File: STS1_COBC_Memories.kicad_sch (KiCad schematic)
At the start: 9 parts, among them J5 Conn_01x03_Male

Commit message: Set all passive components (except in the RF path) to 0603
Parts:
- C3, C4, C5, C6: footprint Capacitor_SMD:C_0805_2012Metric -> Capacitor_SMD:C_0603_1608Metric
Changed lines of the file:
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@@
     (property "Reference" "C3" (id 0) (at 118.11 40.5892 90))
     (property "Value" "100n" (id 1) (at 118.11 42.9006 90))
-    (property "Footprint" "Capacitor_SMD:C_0805_2012Metric" (id 2) (at 114.3 47.9552 0)
+    (property "Footprint" "Capacitor_SMD:C_0603_1608Metric" (id 2) (at 114.3 47.9552 0)
       (effects (font (size 1.27 1.27)) hide)
     )
@@
     (property "Reference" "C4" (id 0) (at 118.11 49.4792 90))
     (property "Value" "47u" (id 1) (at 118.11 51.7906 90))
-    (property "Footprint" "Capacitor_SMD:C_0805_2012Metric" (id 2) (at 114.3 56.8452 0)
+    (property "Footprint" "Capacitor_SMD:C_0603_1608Metric" (id 2) (at 114.3 56.8452 0)
       (effects (font (size 1.27 1.27)) hide)
     )
@@
     (property "Reference" "C5" (id 0) (at 226.06 41.8592 90))
     (property "Value" "100n" (id 1) (at 226.06 44.1706 90))
-    (property "Footprint" "Capacitor_SMD:C_0805_2012Metric" (id 2) (at 222.25 49.2252 0)
+    (property "Footprint" "Capacitor_SMD:C_0603_1608Metric" (id 2) (at 222.25 49.2252 0)
       (effects (font (size 1.27 1.27)) hide)
     )
@@
     (property "Reference" "C6" (id 0) (at 226.06 50.7492 90))
     (property "Value" "47u" (id 1) (at 226.06 53.0606 90))
-    (property "Footprint" "Capacitor_SMD:C_0805_2012Metric" (id 2) (at 222.25 58.1152 0)
+    (property "Footprint" "Capacitor_SMD:C_0603_1608Metric" (id 2) (at 222.25 58.1152 0)
       (effects (font (size 1.27 1.27)) hide)
     )

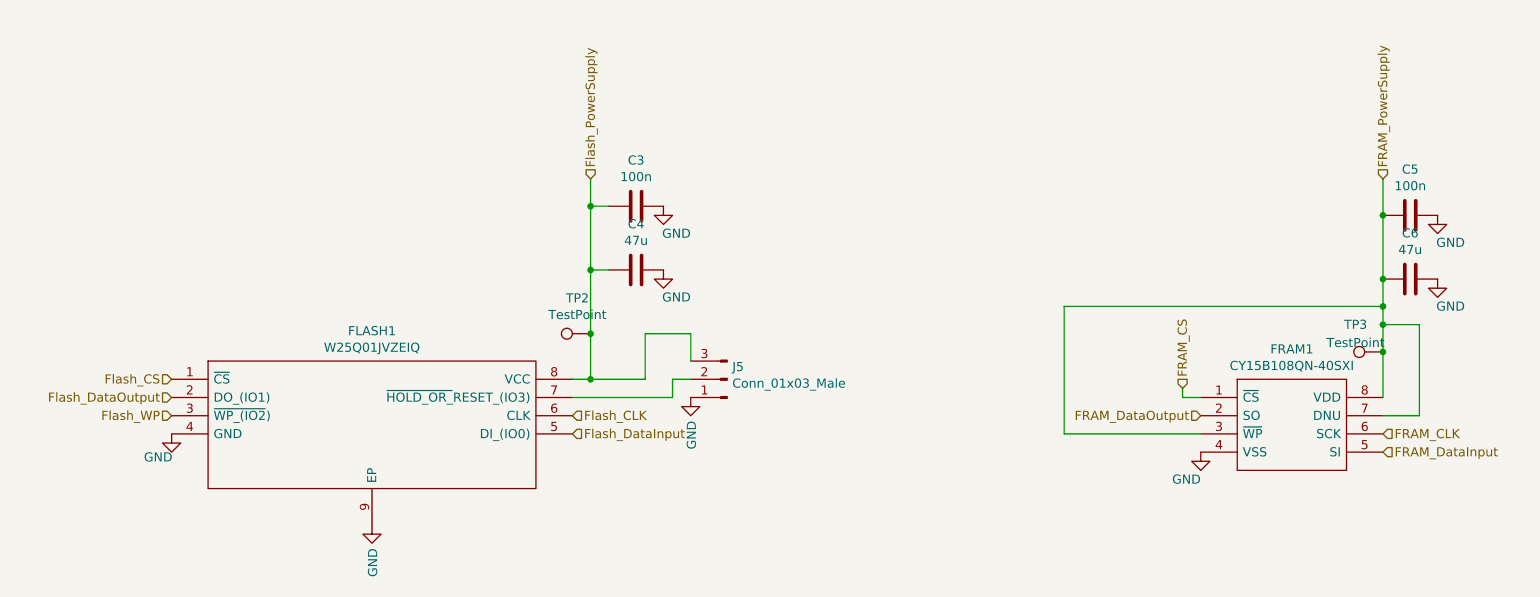
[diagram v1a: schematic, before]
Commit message: feat: clean up schematic
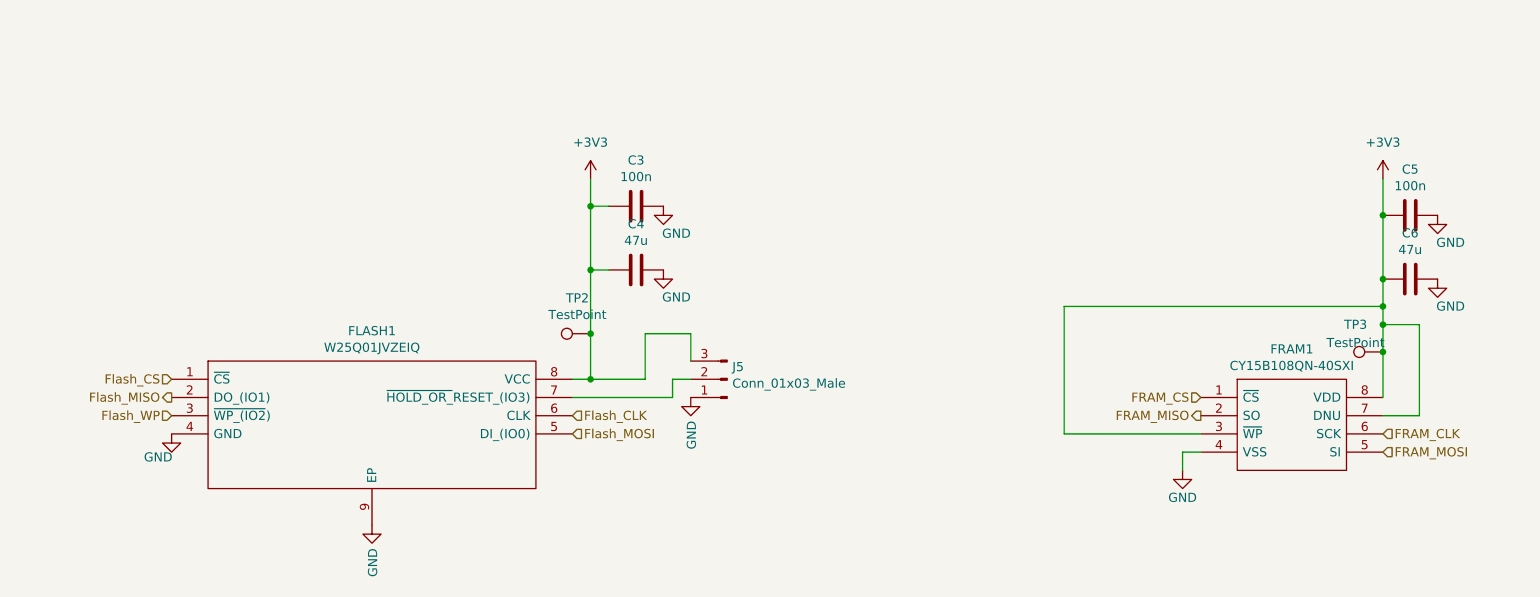
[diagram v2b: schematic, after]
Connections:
- net Flash_PowerSupply is gone; now on net +3V3: C3.2, C4.2, FLASH1.8 (VCC), J5.3 (Pin_3), TP2.1
- net FRAM_DataInput renamed FRAM_MOSI
- net FRAM_DataOutput renamed FRAM_MISO
- net FRAM_PowerSupply renamed +3V3
- net Flash_DataInput renamed Flash_MOSI
- net Flash_DataOutput renamed Flash_MISO
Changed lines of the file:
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@@
-    (stroke (width 0) (type default) (color 0 0 0 0))
-  )
-  (wire (pts (xy 196.85 73.66) (xy 194.31 73.66))
     (stroke (width 0) (type default) (color 0 0 0 0))
   )
@@
     (stroke (width 0) (type default) (color 0 0 0 0))
   )
+  (wire (pts (xy 194.31 81.28) (xy 196.85 81.28))
+    (stroke (width 0) (type default) (color 0 0 0 0))
+  )
   (wire (pts (xy 177.8 78.74) (xy 196.85 78.74))
     (stroke (width 0) (type default) (color 0 0 0 0))
@@
     (stroke (width 0) (type default) (color 0 0 0 0))
   )
-  (wire (pts (xy 194.31 72.39) (xy 194.31 73.66))
-    (stroke (width 0) (type default) (color 0 0 0 0))
-  )
   (wire (pts (xy 125.73 68.58) (xy 125.73 64.77))
     (stroke (width 0) (type default) (color 0 0 0 0))
@@
     (stroke (width 0) (type default) (color 0 0 0 0))
   )
+  (wire (pts (xy 194.31 83.82) (xy 194.31 81.28))
+    (stroke (width 0) (type default) (color 0 0 0 0))
+  )
   (wire (pts (xy 119.38 64.77) (xy 119.38 71.12))
     (stroke (width 0) (type default) (color 0 0 0 0))
@@
     (stroke (width 0) (type default) (color 0 0 0 0))
   )
-  (hierarchical_label "FRAM_CS" (shape input) (at 194.31 72.39 90)
+  (hierarchical_label "FRAM_CS" (shape input) (at 196.85 73.66 180)
+    (effects (font (size 1.27 1.27)) (justify right))
+  )
+  (hierarchical_label "FRAM_MOSI" (shape input) (at 222.25 81.28 0)
     (effects (font (size 1.27 1.27)) (justify left))
   )
-  (hierarchical_label "FRAM_PowerSupply" (shape input) (at 222.25 43.18 90)
-    (effects (font (size 1.27 1.27)) (justify left))
-  )
-  (hierarchical_label "FRAM_DataInput" (shape input) (at 222.25 81.28 0)
-    (effects (font (size 1.27 1.27)) (justify left))
-  )
-  (hierarchical_label "Flash_DataInput" (shape input) (at 109.22 78.74 0)
+  (hierarchical_label "Flash_MOSI" (shape input) (at 109.22 78.74 0)
     (effects (font (size 1.27 1.27)) (justify left))
   )
@@
     (effects (font (size 1.27 1.27)) (justify left))
   )
-  (hierarchical_label "Flash_DataOutput" (shape input) (at 53.34 73.66 180)
+  (hierarchical_label "Flash_MISO" (shape output) (at 53.34 73.66 180)
     (effects (font (size 1.27 1.27)) (justify right))
   )
@@
     (effects (font (size 1.27 1.27)) (justify right))
   )
-  (hierarchical_label "FRAM_DataOutput" (shape input) (at 196.85 76.2 180)
+  (hierarchical_label "FRAM_MISO" (shape output) (at 196.85 76.2 180)
     (effects (font (size 1.27 1.27)) (justify right))
   )
-  (hierarchical_label "Flash_PowerSupply" (shape input) (at 111.76 43.18 90)
-    (effects (font (size 1.27 1.27)) (justify left))
-  )
   (symbol (lib_id "power:GND") (at 53.34 78.74 0) (unit 1)
     (in_bom yes) (on_board yes)
@@
     (pin "1")
   )
-  (symbol (lib_id "power:GND") (at 196.85 81.28 0) (unit 1)
-    (in_bom yes) (on_board yes)
-    (property "Reference" "#PWR021" (id 0) (at 196.85 87.63 0)
-      (effects (font (size 1.27 1.27)) hide)
-    )
-    (property "Value" "GND" (id 1) (at 196.85 85.09 0)
-      (effects (font (size 1.27 1.27)) (justify right))
-    )
-    (property "Footprint" "" (id 2) (at 196.85 81.28 0)
-      (effects (font (size 1.27 1.27)) hide)
-    )
-    (property "Datasheet" "" (id 3) (at 196.85 81.28 0)
+  (symbol (lib_name "GND_3") (lib_id "power:GND") (at 194.31 83.82 0) (unit 1)
+    (in_bom yes) (on_board yes)
+    (property "Reference" "#PWR021" (id 0) (at 194.31 90.17 0)
+      (effects (font (size 1.27 1.27)) hide)
+    )
+    (property "Value" "GND" (id 1) (at 194.31 87.63 0))
+    (property "Footprint" "" (id 2) (at 194.31 83.82 0)
+      (effects (font (size 1.27 1.27)) hide)
+    )
+    (property "Datasheet" "" (id 3) (at 194.31 83.82 0)
       (effects (font (size 1.27 1.27)) hide)
     )
@@
     (pin "2")
   )
-  (symbol (lib_id "power:GND") (at 121.92 55.88 0) (unit 1)
+  (symbol (lib_name "GND_5") (lib_id "power:GND") (at 121.92 55.88 0) (unit 1)
     (in_bom yes) (on_board yes)
     (property "Reference" "#PWR019" (id 0) (at 121.92 62.23 0)
@@
     (pin "1")
   )
-  (symbol (lib_id "power:GND") (at 121.92 46.99 0) (unit 1)
+  (symbol (lib_name "GND_6") (lib_id "power:GND") (at 121.92 46.99 0) (unit 1)
     (in_bom yes) (on_board yes)
     (property "Reference" "#PWR018" (id 0) (at 121.92 53.34 0)
@@
     (pin "2")
   )
-  (symbol (lib_id "power:GND") (at 229.87 57.15 0) (unit 1)
+  (symbol (lib_name "GND_1") (lib_id "power:GND") (at 229.87 57.15 0) (unit 1)
     (in_bom yes) (on_board yes)
     (property "Reference" "#PWR023" (id 0) (at 229.87 63.5 0)
@@
     (pin "1")
   )
-  (symbol (lib_id "power:GND") (at 229.87 48.26 0) (unit 1)
+  (symbol (lib_name "GND_2") (lib_id "power:GND") (at 229.87 48.26 0) (unit 1)
     (in_bom yes) (on_board yes)
     (property "Reference" "#PWR022" (id 0) (at 229.87 54.61 0)
@@
     (pin "1")
   )
-  (symbol (lib_id "power:GND") (at 125.73 73.66 0) (unit 1)
+  (symbol (lib_name "GND_4") (lib_id "power:GND") (at 125.73 73.66 0) (unit 1)
     (in_bom yes) (on_board yes)
     (property "Reference" "#PWR020" (id 0) (at 125.73 80.01 0)
@@
     (pin "1")
   )
-  (symbol (lib_id "power:GND") (at 81.28 91.44 0) (unit 1)
+  (symbol (lib_id "power:+3V3") (at 111.76 43.18 0) (unit 1)
+    (in_bom yes) (on_board yes) (fields_autoplaced)
+    (property "Reference" "#PWR?" (id 0) (at 111.76 46.99 0)
+      (effects (font (size 1.27 1.27)) hide)
+    )
+    (property "Value" "+3V3" (id 1) (at 111.76 38.1 0))
+    (property "Footprint" "" (id 2) (at 111.76 43.18 0)
+      (effects (font (size 1.27 1.27)) hide)
+    )
+    (property "Datasheet" "" (id 3) (at 111.76 43.18 0)
+      (effects (font (size 1.27 1.27)) hide)
+    )
+    (pin "1")
+  )
+  (symbol (lib_name "GND_7") (lib_id "power:GND") (at 81.28 91.44 0) (unit 1)
     (in_bom yes) (on_board yes)
     (property "Reference" "#PWR0131" (id 0) (at 81.28 97.79 0)
@@
       (effects (font (size 1.27 1.27)) hide)
     )
+    (pin "1")
+  )
+  (symbol (lib_id "power:+3V3") (at 222.25 43.18 0) (unit 1)
+    (in_bom yes) (on_board yes) (fields_autoplaced)
+    (property "Reference" "#PWR?" (id 0) (at 222.25 46.99 0)
+      (effects (font (size 1.27 1.27)) hide)
+    )
+    (property "Value" "+3V3" (id 1) (at 222.25 38.1 0))
+    (property "Footprint" "" (id 2) (at 222.25 43.18 0)
+      (effects (font (size 1.27 1.27)) hide)
+    )
+    (property "Datasheet" "" (id 3) (at 222.25 43.18 0)
+      (effects (font (size 1.27 1.27)) hide)
+    )

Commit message: feat: more schematic cleanup
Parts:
- removed TP2, TP3: TestPoint, STS1library:STS1_Testpoint, symbol Connector:TestPoint
- C4: value 47u -> 47µ
- J5: value Conn_01x03_Male -> Flash_Dbg
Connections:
- net Flash_WP renamed Flash_~{WP}
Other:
- moved on the sheet: C3, C4, C5, C6, J5

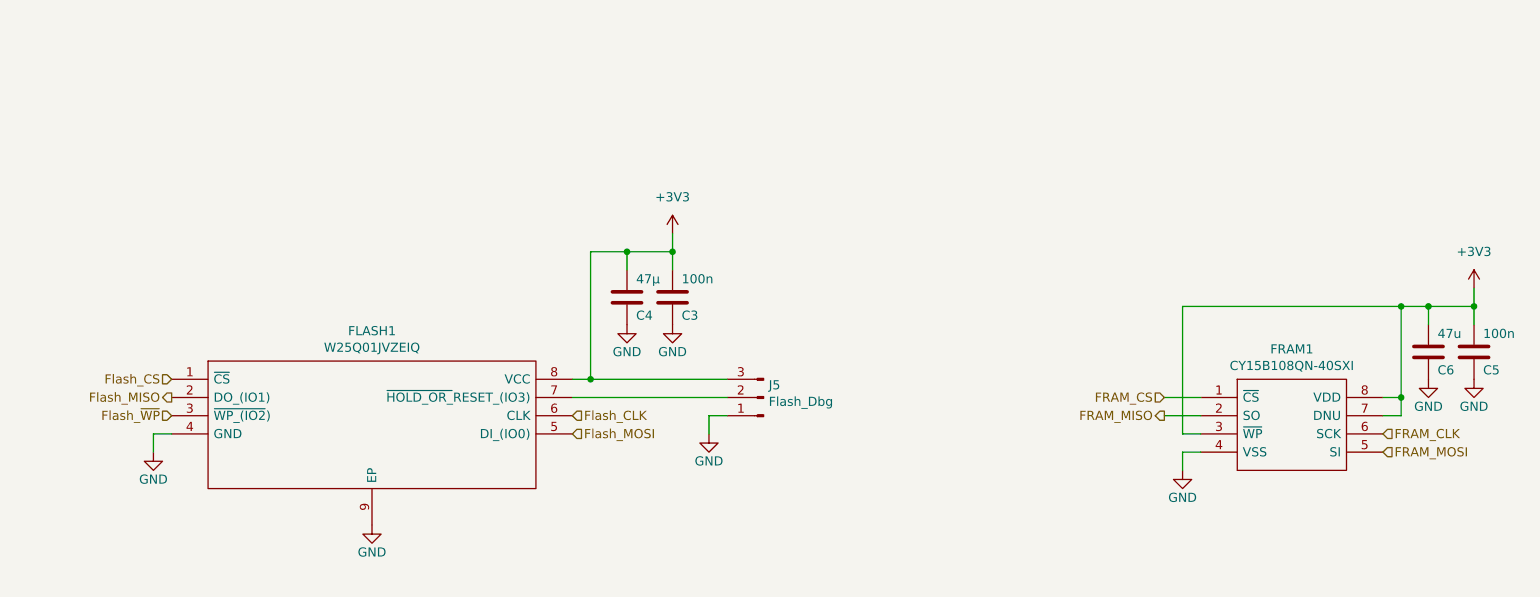
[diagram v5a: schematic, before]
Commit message: Exclude jumpers, mounting holes, fiducials etc. from BOM
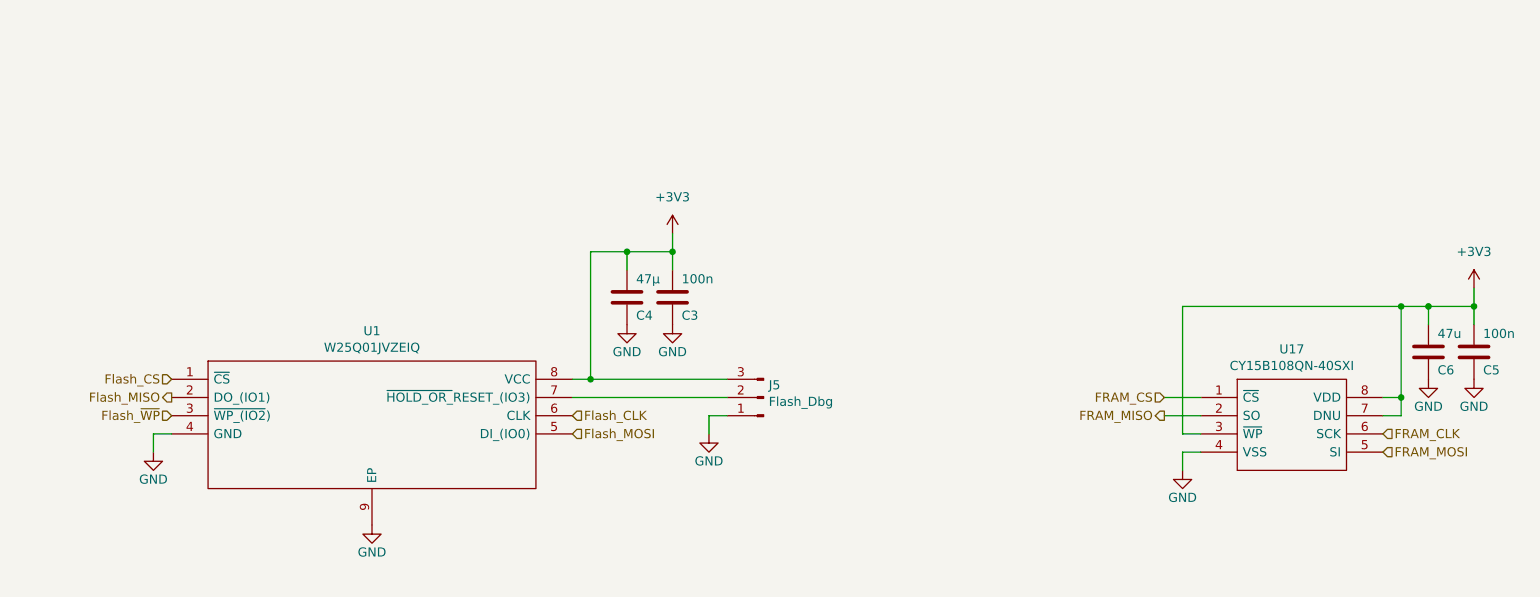
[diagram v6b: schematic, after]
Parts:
- renumbered FLASH1 to U1, FRAM1 to U17
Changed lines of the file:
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@@
   (symbol (lib_id "STS1_COBC_V2-rescue:W25Q01JVZEIQ-W25Q01JVZEIQ") (at 53.34 71.12 0) (unit 1)
     (in_bom yes) (on_board yes)
-    (property "Reference" "FLASH1" (id 0) (at 81.28 64.389 0))
+    (property "Reference" "U1" (id 0) (at 81.28 64.389 0))
     (property "Value" "W25Q01JVZEIQ" (id 1) (at 81.28 66.7004 0))
     (property "Footprint" "STSLib:SON127P800X600X80-9N-D" (id 2) (at 105.41 68.58 0)
@@
   (symbol (lib_id "STS1_COBC_V2-rescue:CY15B108QN-40SXI-CY15B108QN-40SXI") (at 196.85 73.66 0) (unit 1)
     (in_bom yes) (on_board yes)
-    (property "Reference" "FRAM1" (id 0) (at 209.55 66.929 0))
+    (property "Reference" "U17" (id 0) (at 209.55 66.929 0))
     (property "Value" "CY15B108QN-40SXI" (id 1) (at 209.55 69.2404 0))
     (property "Footprint" "STSLib:SOIC127P800X203-8N" (id 2) (at 218.44 71.12 0)
